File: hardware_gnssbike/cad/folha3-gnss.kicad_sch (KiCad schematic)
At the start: 9 parts, among them U301 u-blox MAX-F10S, U302 TI TXU0204BQAR

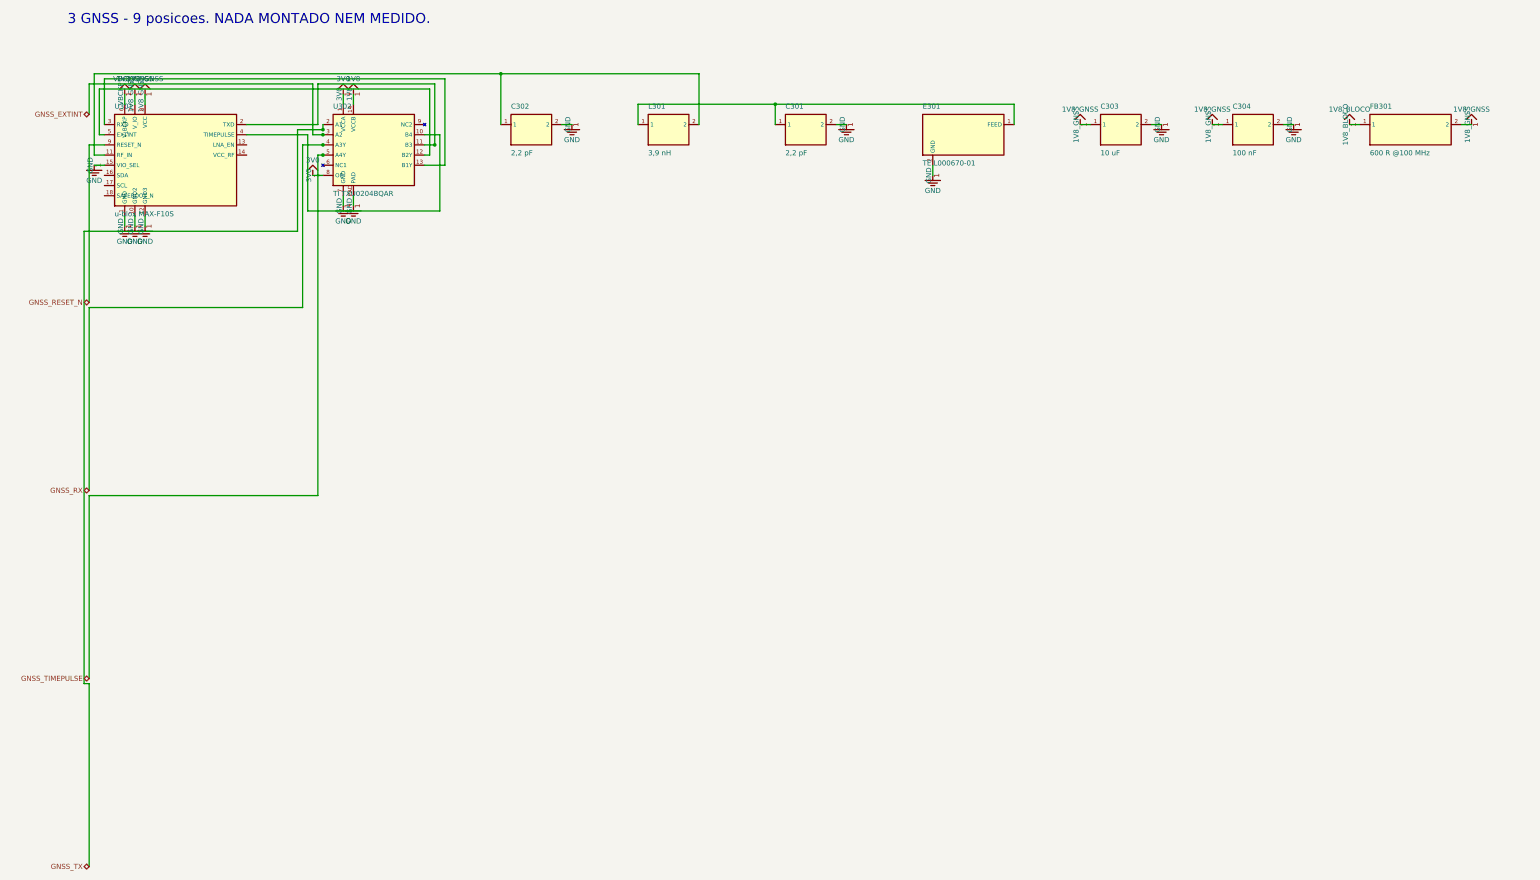
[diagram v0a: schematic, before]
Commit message: fix(hardware): the solar panel and the antenna had nowhere to touch the board
This board could not be built. The six solar modules live in the case and
connect to SRC and GND; the GNSS antenna element lives in the case wall and
connects to RF_ANT and GND. On the board, SRC reached only the harvester, its
capacitor and its inductor, and RF_ANT reached only the pi network. There was
no pad for either of them. The wires had nowhere to land.

04-pcb-e-caixa.md had already decided how they arrive - the antenna "com
contatos de mola" on line 271, the panels "em 3 grupos, mola ou FPC" on line
388 - and line 661 listed as open that "a area dos pads de mola e dos
conectores dos tres grupos de paineis nao esta dimensionada em lugar nenhum".
It is dimensioned now: two 2.0 x 2.0 mm gold pads at 3.0 mm pitch, with no
paste, because a spring presses on them and nothing is soldered.

J302 takes the antenna, just below its keep-out and a few millimetres from
the pi network, which is what the same document asks for when it says the
50 ohm line is "poucos mm". J103, J104 and J105 take the three groups of
panels, in the free bands of the two edges - computed, not guessed: the left
edge is taken by the light sensor, the two flat cables, the M2 hole, the
battery connector and a key. All three sit within about 15 mm of the
harvester, because SRC comes off a solar cell at high impedance and a long
run of it picks up everything.

The bodies stopped being identical black cuboids. What distinguishes these
packages at a glance is where the metal is, so a QFN now shows its exposed
pad and the ring of lead flags underneath, a SOIC stands on gull-wing leads
that reach out on two sides, a SOT has its three, and a wafer-level package
is bare silicon over a grid of balls. Each one carries the pin 1 dot. Every
dimension comes from the outline the footprint already had; what is new is
only which part of it is drawn as metal.

116 parts, no DRC error, 131 connections routed, and twelve of the thirteen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
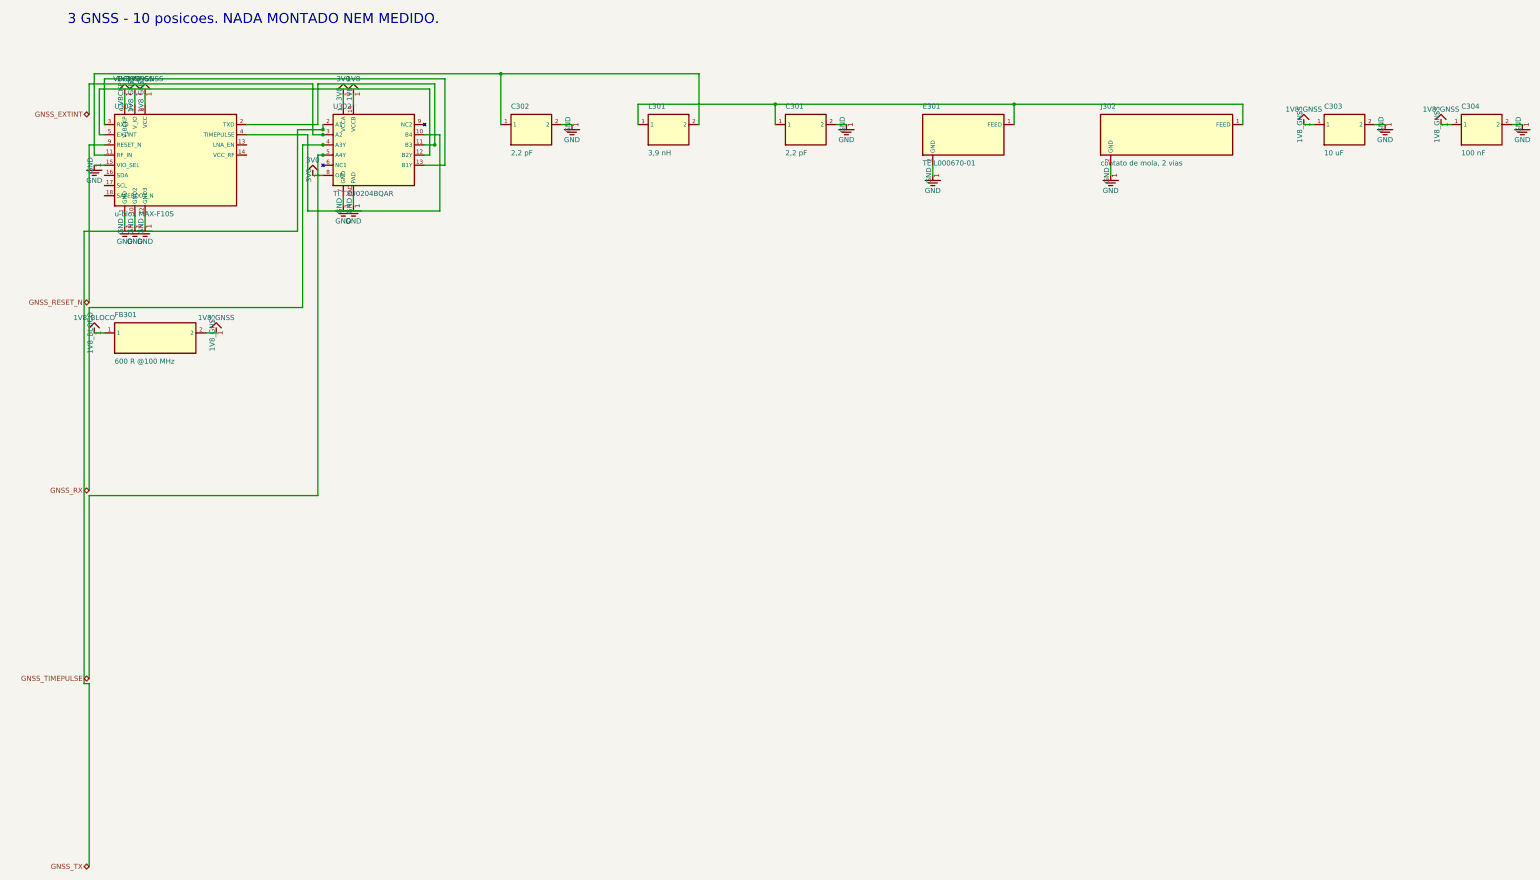
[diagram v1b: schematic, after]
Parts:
- added J302: contato de mola, 2 vias, gnssbike:ContatoMola_2x2mm_P3mm, symbol gnssbike:J302
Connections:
- net GND: now also J302.2 (GND)
- net at C301.1, E301.1 (FEED), L301.1: now also J302.1 (FEED)
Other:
- note added: "3 GNSS - 10 posicoes. NADA MONTADO NEM MEDIDO."
- note removed: "3 GNSS - 9 posicoes. NADA MONTADO NEM MEDIDO."
- moved on the sheet: C303, C304, FB301

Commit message: feat(hardware): the test points, a readable silkscreen, and paper that fits
Eleven of the sixteen test points of 06-conectores-e-pontos-de-teste.md were
not on the board. Only the three of the console sheet existed; a rail you
cannot put a probe on is a rail you cannot debug. VBUS, VBUSOUT, VBAT, VSYS,
3V0, 1V8, SD3V0, 3V3BL, VBCKP, VINT and the ground reference are there now,
each beside the thing it measures, and each takes what is LEFT: placed with
the rest of JUNTO they pushed three decoupling capacitors off their rings,
one of them to 4.0 mm from a pin that wants 2. The two that are still
missing are the document's own absences - TP111 measures ST_STO, which the
AEM10900 datasheet does not have, and TP401 measures 5V0, from a regulator
not fitted with the JDI panel. The list lives in parts.TESTE and nets.py
refuses a point that names a net that does not exist.

The silkscreen named nothing. Every reference sat 1.8 mm above its part at
0.7 mm with a 0.1 mm stroke - below the floor every fab publishes - and 37
pairs of designators printed on top of each other. The text is at the fab
minimum now, 0.8 mm with 0.15, and each label is PLACED: candidates around
its own courtyard, nearest first, never over another label and preferably
not over another part's outline. 127 references, 0 overlapping. The mounting
hole's REF** is hidden; it names nothing and was the last label sitting on
another.

Ground: a mesh, not just a hem. Edge stitching keeps the boundary of the
surface pours from becoming a radiating slot and does nothing for the
middle, where a patch of pour that reaches the inner plane through a via
20 mm away is not ground at 2.4 GHz. A 4.0 mm grid of ground vias now
covers the board - under the 6.1 mm that is a tenth of a wavelength in
FR-4 - laid last, on what is free, so a stitch never costs a connection.

The router's search learned about pad fields. The neck beside a pad existed
only in emitir(), and emitir only ever sees paths the search already found,
so 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
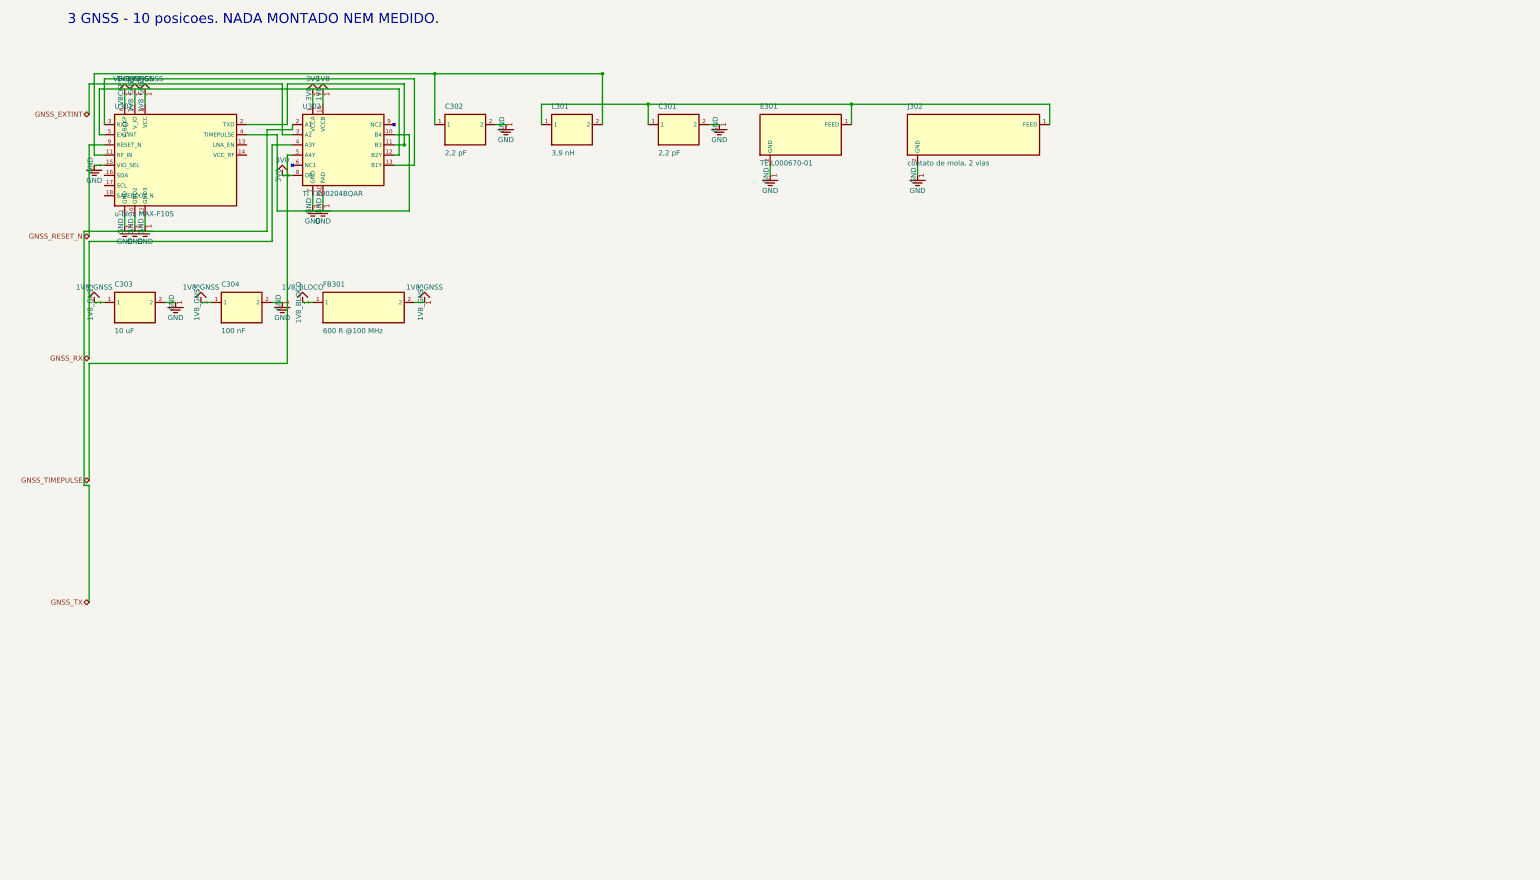
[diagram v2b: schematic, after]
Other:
- moved on the sheet: C301, C302, C303, C304, E301, FB301, J302, L301, U302

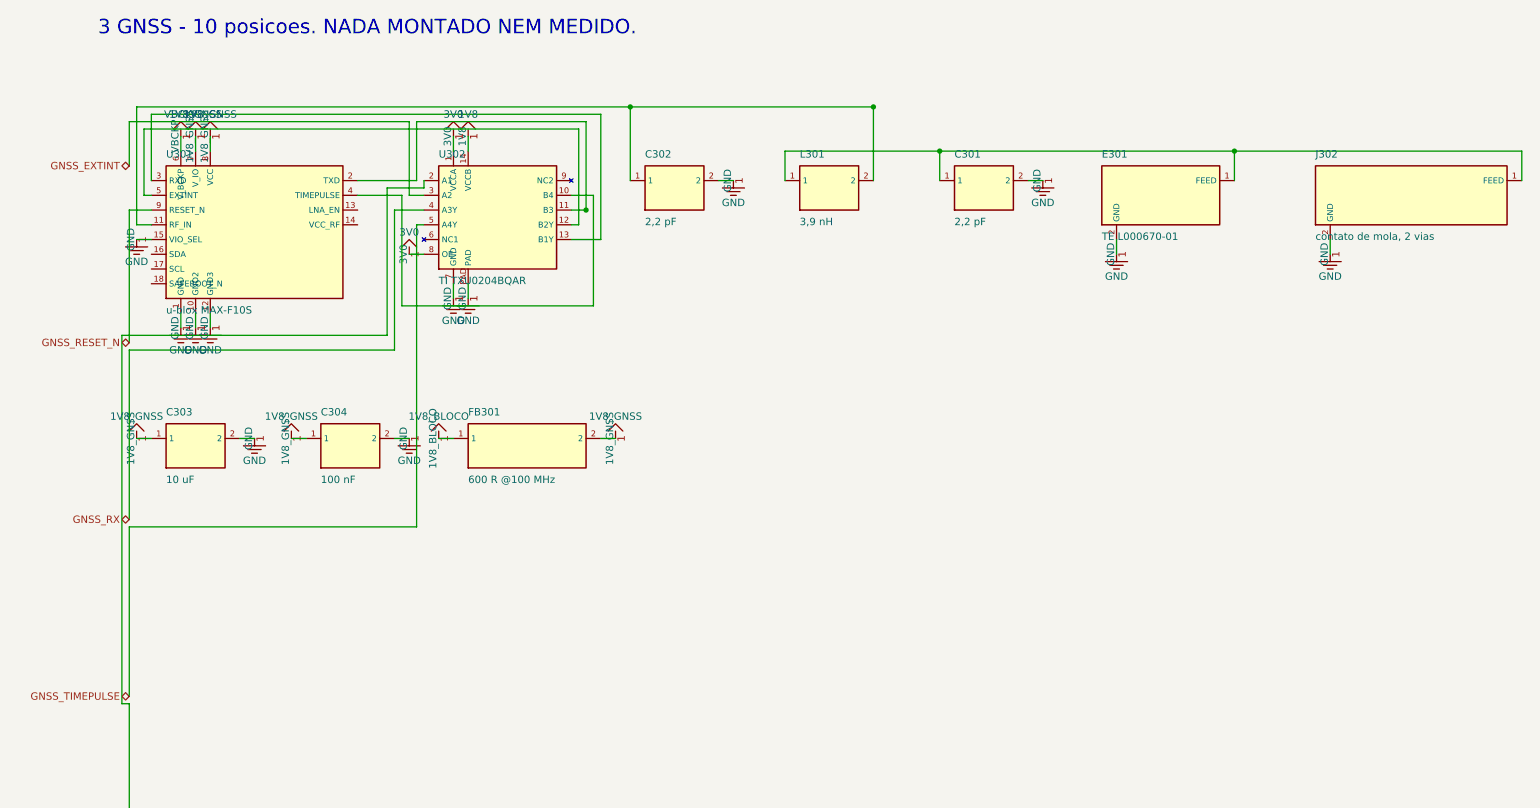
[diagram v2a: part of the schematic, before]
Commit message: feat(hardware): draw each part as its own symbol, not as a block
A rectangle with pin names down its sides is how an INTEGRATED CIRCUIT is
drawn, and only an integrated circuit. This generator drew all 127 parts
that way - resistors, ceramic capacitors, diodes, the TVS - and a sheet of
blocks joined by lines does not show a circuit.

Every class has its own symbol now, in the standard form, with the lead
axis on x and the body between -1.27 and +1.27 mm: a zigzag for a resistor
and a 0 ohm link (42 of them), two parallel plates for a ceramic capacitor
and a curved plate with a + for an electrolytic (31), four arcs for an
inductor (4), the same arcs inside a rectangle for a ferrite bead, which is
what tells the two apart, a zigzag with a diagonal arrow for the thermistor,
a triangle and a bar for a diode with arrows leaving it for an LED, two
contacts with a bar and a plunger for a key, a circle with a diagonal for
the buzzer, and a circle on the end of a lead for a test point. The 36 that
stay rectangles are the ones that should be: the ICs, the connectors and the
display. A two terminal part no longer prints pin numbers or pin names -
"1" and "2" on a resistor is noise, and the symbol already says which end is
which where it matters.

The power symbols had room reserved for the symbol and none for its NAME:
two ground pins two grid steps apart each got their own symbol, the symbols
did not collide, and the words printed over each other - "GNDGNDGND" along
the bottom of every chip. What is reserved now is the whole thing. With a
limit: the first cut let the stub run to fourteen grid steps looking for a
clear spot, and one of them crossed a component and split a net. A long stub
is worse than a crowded label, so it stops at eight and the label gives way.

One attempt is NOT in this commit, on purpose. Grouping every pin of a rail
on one edge into a single symbol - which is what a person draws - joins the
stubs with a line that runs along the part's edge and crosses w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
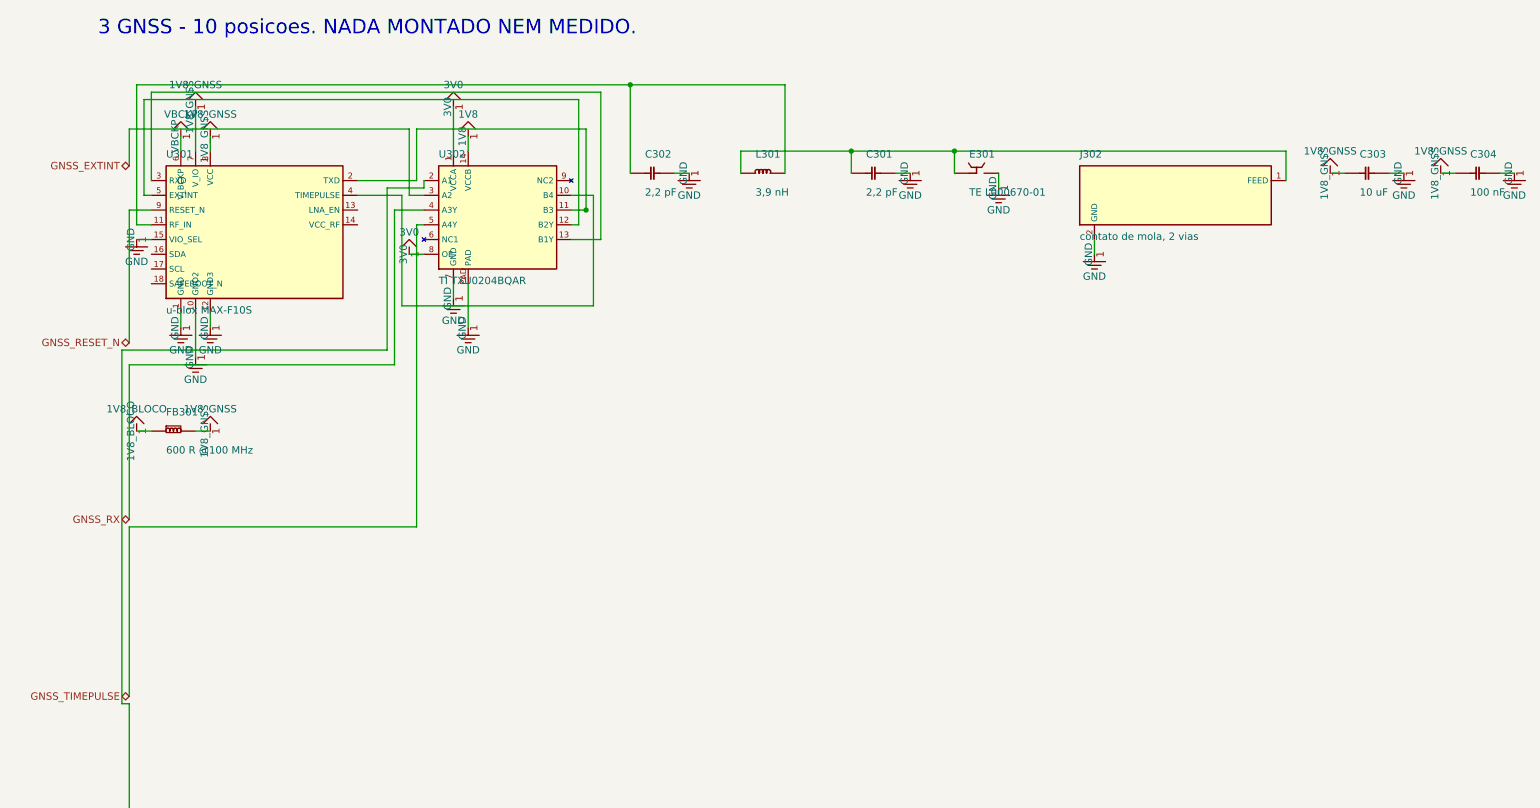
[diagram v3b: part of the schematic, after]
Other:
- moved on the sheet: J302
